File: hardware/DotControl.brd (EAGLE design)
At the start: 30.7 x 65 mm, 24 parts, among them CN1 1X4-BIG, J3 USB-MICROB, SW2 Previous, SW5 Previous, SW6 Next, SW8 Ok, U1 ATMEGA328P-MU-QFN32, U2 TMP102

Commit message: Minor rearrange wires
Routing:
- net +3V3: track 156.8 -> 151.4 mm
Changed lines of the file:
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@@
 <layer number="14" name="Route14" color="1" fill="6" visible="no" active="no"/>
 <layer number="15" name="Route15" color="4" fill="6" visible="no" active="no"/>
-<layer number="16" name="Bottom" color="1" fill="1" visible="no" active="yes"/>
+<layer number="16" name="Bottom" color="1" fill="1" visible="yes" active="yes"/>
 <layer number="17" name="Pads" color="2" fill="1" visible="yes" active="yes"/>
 <layer number="18" name="Vias" color="2" fill="1" visible="yes" active="yes"/>
@@
 <layer number="20" name="Dimension" color="15" fill="1" visible="yes" active="yes"/>
 <layer number="21" name="tPlace" color="7" fill="1" visible="yes" active="yes"/>
-<layer number="22" name="bPlace" color="7" fill="1" visible="no" active="yes"/>
-<layer number="23" name="tOrigins" color="15" fill="1" visible="no" active="yes"/>
-<layer number="24" name="bOrigins" color="15" fill="1" visible="no" active="yes"/>
+<layer number="22" name="bPlace" color="7" fill="1" visible="yes" active="yes"/>
+<layer number="23" name="tOrigins" color="15" fill="1" visible="yes" active="yes"/>
+<layer number="24" name="bOrigins" color="15" fill="1" visible="yes" active="yes"/>
 <layer number="25" name="tNames" color="7" fill="1" visible="no" active="yes"/>
 <layer number="26" name="bNames" color="7" fill="1" visible="no" active="yes"/>
@@
 <wire x1="16.891" y1="12.7762" x2="16.5862" y2="13.081" width="0.1524" layer="1"/>
 <wire x1="16.5862" y1="13.081" x2="16.4338" y2="13.081" width="0.1524" layer="1"/>
-<wire x1="19.6592" y1="13.6318" x2="19.194" y2="14.097" width="0.1524" layer="16"/>
-<wire x1="19.194" y1="14.097" x2="18.7452" y2="14.097" width="0.1524" layer="16"/>
+<wire x1="19.6592" y1="13.6318" x2="19.2194" y2="14.0716" width="0.1524" layer="16"/>
 <wire x1="16.8652" y1="13.5124" x2="17.3732" y2="13.5124" width="0.1524" layer="16"/>
 <wire x1="17.3732" y1="13.5124" x2="17.9324" y2="14.0716" width="0.1524" layer="16"/>
-<wire x1="17.9324" y1="14.0716" x2="18.7198" y2="14.0716" width="0.1524" layer="16"/>
-<wire x1="18.7198" y1="14.0716" x2="18.7452" y2="14.097" width="0.1524" layer="16"/>
+<wire x1="17.9324" y1="14.0716" x2="19.2194" y2="14.0716" width="0.1524" layer="16"/>
 </signal>
 <signal name="RST">
@@
 <contactref element="R7" pad="5"/>
 <contactref element="SJ1" pad="2"/>
-<wire x1="26.0604" y1="39.624" x2="26.0604" y2="41.6052" width="0.1524" layer="16"/>
-<wire x1="26.0604" y1="41.6052" x2="26.0604" y2="42.672" width="0.1524" layer="16"/>
-<wire x1="26.9748" y1="38.7096" x2="26.0604" y2="39.624" width="0.1524" layer="16"/>
-<wire x1="26.9748" y1="38.2524" x2="26.9748" y2="38.7096" width="0.1524" layer="16"/>
-<wire x1="26.8224" y1="38.1" x2="26.9748" y2="38.2524" width="0.1524" layer="16"/>
-<wire x1="26.9748" y1="37.9476" x2="26.8224" y2="38.1" width="0.1524" layer="16"/>
 <wire x1="3.2004" y1="61.4172" x2="3.2004" y2="61.8744" width="0.1524" layer="1"/>
 <wire x1="3.6576" y1="60.96" x2="3.2004" y2="61.4172" width="0.1524" layer="1"/>
@@
 <wire x1="12.4968" y1="55.0164" x2="10.0584" y2="55.0164" width="0.1524" layer="1"/>
 <wire x1="25.908" y1="41.6052" x2="12.4968" y2="55.0164" width="0.1524" layer="1"/>
-<wire x1="26.0604" y1="41.6052" x2="25.908" y2="41.6052" width="0.1524" layer="16"/>
 <wire x1="3.2004" y1="61.8744" x2="3.1225" y2="61.9" width="0.1524" layer="1"/>
 <wire x1="13.8684" y1="23.7744" x2="13.2588" y2="23.7744" width="0.1524" layer="16"/>

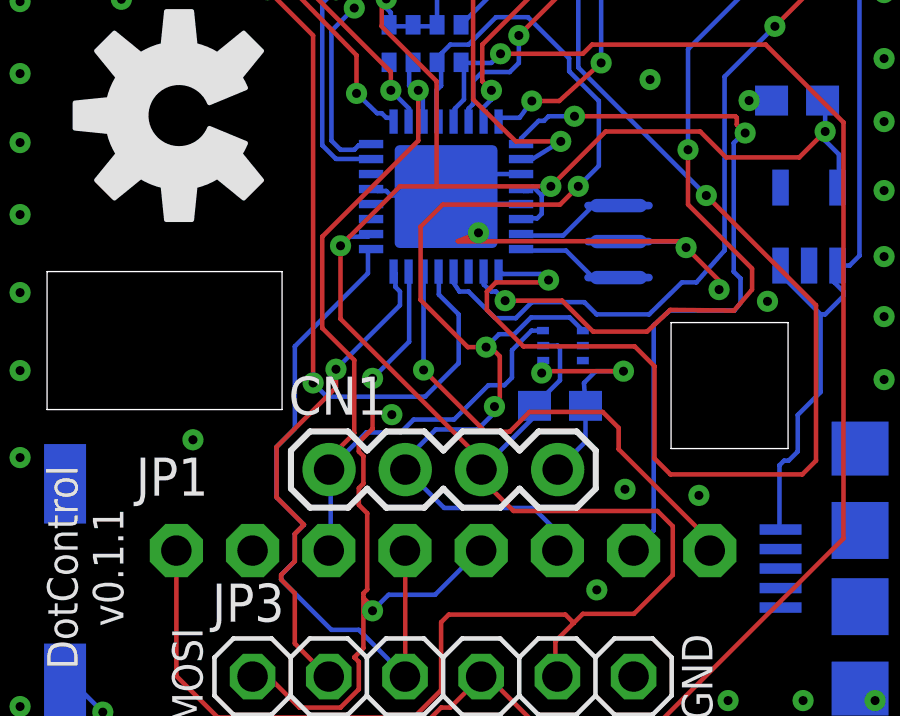
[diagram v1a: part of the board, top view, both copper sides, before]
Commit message: Improve routing and vias
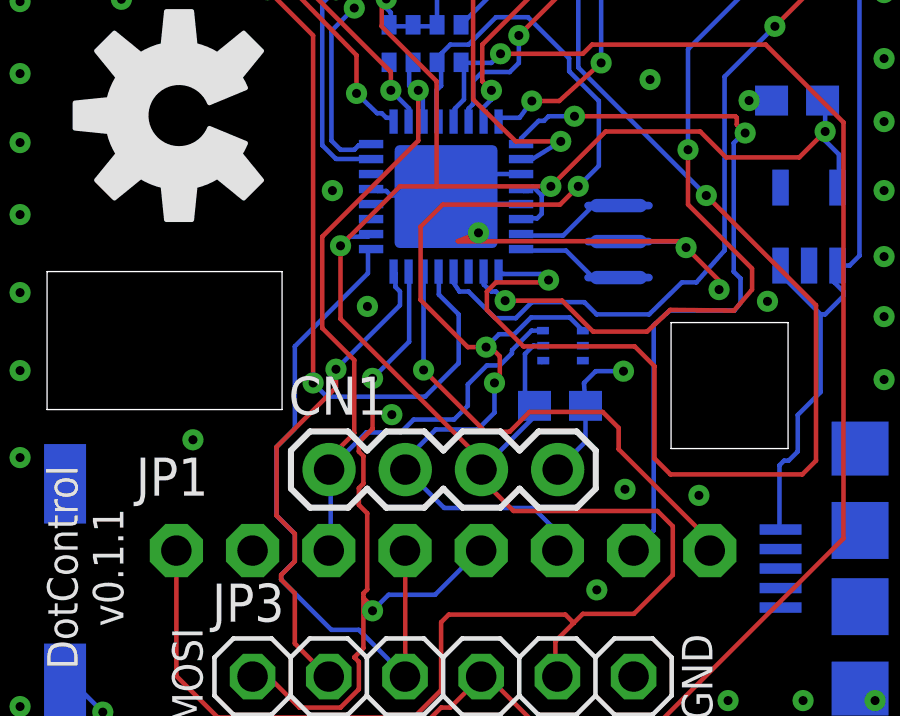
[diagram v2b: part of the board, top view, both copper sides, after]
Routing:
- net GND: track 34.6 -> 31.5 mm, vias 103 -> 104
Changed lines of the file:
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@@
 <wire x1="15.4432" y1="17.0372" x2="16.256" y2="17.85" width="0.1524" layer="16"/>
 <wire x1="18.3392" y1="12.6318" x2="18.288" y2="12.5806" width="0.1524" layer="16"/>
-<wire x1="18.288" y1="12.5806" x2="18.288" y2="12.2174" width="0.1524" layer="16"/>
-<via x="18.288" y="12.2174" extent="1-16" drill="0.3"/>
-<wire x1="18.288" y1="12.2174" x2="18.35" y2="12.2794" width="0.1524" layer="1"/>
-<wire x1="18.35" y1="12.2794" x2="21.0132" y2="12.2794" width="0.1524" layer="1"/>
 <wire x1="19.6968" y1="11.8876" x2="20.0886" y2="12.2794" width="0.1524" layer="16"/>
 <wire x1="20.0886" y1="12.2794" x2="21.0132" y2="12.2794" width="0.1524" layer="16"/>
+<via x="12.4788" y="14.4384" extent="1-16" drill="0.3"/>
+<via x="11.3104" y="18.2992" extent="1-16" drill="0.3"/>
 <wire x1="16.256" y1="17.85" x2="16.1798" y2="17.8308" width="0" layer="19" extent="16-16"/>
 </signal>
@@
 <wire x1="10.0584" y1="10.3632" x2="10.0584" y2="13.1064" width="0.1524" layer="16"/>
 <wire x1="9.4488" y1="9.7536" x2="10.0584" y2="10.3632" width="0.1524" layer="16"/>
-<wire x1="9.4488" y1="8.0772" x2="9.4488" y2="9.7536" width="0.1524" layer="16"/>
-<wire x1="10.3632" y1="7.1628" x2="9.4488" y2="8.0772" width="0.1524" layer="16"/>
-<wire x1="10.0584" y1="6.858" x2="10.3632" y2="7.1628" width="0.1524" layer="16"/>
+<wire x1="9.4488" y1="7.4676" x2="9.4488" y2="9.7536" width="0.1524" layer="16"/>
 <wire x1="10.0584" y1="5.9436" x2="10.0584" y2="6.858" width="0.1524" layer="16"/>
 <wire x1="9.6012" y1="5.4864" x2="10.0584" y2="5.9436" width="0.1524" layer="16"/>
@@
 <wire x1="12.4968" y1="16.3068" x2="12.6" y2="16.35" width="0.1524" layer="16"/>
 <wire x1="13.716" y1="2.1336" x2="13.73" y2="2.1" width="0.1524" layer="16"/>
+<wire x1="9.4488" y1="7.4676" x2="10.0584" y2="6.858" width="0.1524" layer="16"/>
 </signal>
 <signal name="MISO">
@@
 <wire x1="13.5636" y1="14.9352" x2="13.4112" y2="15.0876" width="0.1524" layer="16"/>
 <wire x1="13.5636" y1="14.478" x2="13.5636" y2="14.9352" width="0.1524" layer="16"/>
-<wire x1="11.43" y1="12.3444" x2="13.5636" y2="14.478" width="0.1524" layer="16"/>
 <wire x1="11.43" y1="11.7348" x2="11.43" y2="12.3444" width="0.1524" layer="1"/>
 <wire x1="9.4488" y1="9.7536" x2="11.43" y2="11.7348" width="0.1524" layer="1"/>
-<wire x1="9.4488" y1="8.0772" x2="9.4488" y2="9.7536" width="0.1524" layer="1"/>
-<wire x1="10.3632" y1="7.1628" x2="9.4488" y2="8.0772" width="0.1524" layer="1"/>
-<wire x1="10.0584" y1="6.858" x2="10.3632" y2="7.1628" width="0.1524" layer="1"/>
+<wire x1="9.4488" y1="7.4676" x2="9.4488" y2="9.7536" width="0.1524" layer="1"/>
 <wire x1="10.0584" y1="5.9436" x2="10.0584" y2="6.858" width="0.1524" layer="1"/>
 <wire x1="9.6012" y1="5.4864" x2="10.0584" y2="5.9436" width="0.1524" layer="1"/>
@@
 <wire x1="11.1252" y1="2.1336" x2="11.19" y2="2.1" width="0.1524" layer="1"/>
 <via x="11.43" y="12.3444" extent="1-16" drill="0.3"/>
+<wire x1="11.43" y1="12.3444" x2="13.5636" y2="14.478" width="0.1524" layer="16"/>
+<wire x1="9.4488" y1="7.4676" x2="10.0584" y2="6.858" width="0.1524" layer="1"/>
 </signal>
 <signal name="SDA">
@@
 <contactref element="U2" pad="6"/>
 <wire x1="12.4362" y1="10.2362" x2="11.2" y2="9" width="0.1524" layer="16"/>
-<wire x1="17.2974" y1="12.065" x2="17.0434" y2="11.811" width="0.1524" layer="16"/>
-<wire x1="17.0434" y1="11.811" x2="16.51" y2="11.811" width="0.1524" layer="16"/>
-<wire x1="16.51" y1="11.811" x2="15.367" y2="10.668" width="0.1524" layer="16"/>
 <wire x1="15.367" y1="10.668" x2="14.0208" y2="10.668" width="0.1524" layer="16"/>
 <wire x1="14.0208" y1="10.668" x2="13.589" y2="10.2362" width="0.1524" layer="16"/>
@@
 <wire x1="17.9498" y1="13.6318" x2="18.3292" y2="13.6318" width="0.1524" layer="16"/>
 <wire x1="17.9498" y1="13.6318" x2="17.2974" y2="12.9794" width="0.1524" layer="16"/>
-<wire x1="17.2974" y1="12.9794" x2="17.2974" y2="12.065" width="0.1524" layer="16"/>
+<wire x1="17.2974" y1="12.9794" x2="17.2974" y2="12.8778" width="0.1524" layer="16"/>
+<wire x1="17.2974" y1="12.8778" x2="16.891" y2="12.4714" width="0.1524" layer="16"/>
+<wire x1="16.891" y1="12.4714" x2="16.4592" y2="12.4714" width="0.1524" layer="16"/>
+<wire x1="16.4592" y1="12.4714" x2="15.8242" y2="11.8364" width="0.1524" layer="16"/>
+<wire x1="15.8242" y1="11.8364" x2="15.8242" y2="11.1252" width="0.1524" layer="16"/>
+<wire x1="15.8242" y1="11.1252" x2="15.367" y2="10.668" width="0.1524" layer="16"/>
 </signal>
 <signal name="SCL">
@@
 <wire x1="14.7574" y1="10.3378" x2="16.1544" y2="10.3378" width="0.1524" layer="16"/>
 <wire x1="16.1544" y1="10.3378" x2="16.7132" y2="10.8966" width="0.1524" layer="16"/>
-<wire x1="16.7132" y1="10.8966" x2="16.7132" y2="11.0998" width="0.1524" layer="16"/>
-<via x="16.7132" y="11.0998" extent="1-16" drill="0.3"/>
-<wire x1="16.7132" y1="11.0998" x2="16.891" y2="11.2776" width="0.1524" layer="1"/>
-<wire x1="16.891" y1="11.2776" x2="16.891" y2="12.7762" width="0.1524" layer="1"/>
-<wire x1="16.891" y1="12.7762" x2="16.5862" y2="13.081" width="0.1524" layer="1"/>
+<wire x1="16.7132" y1="10.8966" x2="16.7132" y2="11.8872" width="0.1524" layer="16"/>
+<via x="16.7132" y="11.8872" extent="1-16" drill="0.3"/>
 <wire x1="16.5862" y1="13.081" x2="16.4338" y2="13.081" width="0.1524" layer="1"/>
 <wire x1="19.6592" y1="13.6318" x2="19.2194" y2="14.0716" width="0.1524" layer="16"/>
@@
 <wire x1="17.3732" y1="13.5124" x2="17.9324" y2="14.0716" width="0.1524" layer="16"/>
 <wire x1="17.9324" y1="14.0716" x2="19.2194" y2="14.0716" width="0.1524" layer="16"/>
+<wire x1="16.891" y1="12.7762" x2="16.5862" y2="13.081" width="0.1524" layer="1"/>
+<wire x1="16.891" y1="12.7762" x2="16.891" y2="12.065" width="0.1524" layer="1"/>
+<wire x1="16.891" y1="12.065" x2="16.7132" y2="11.8872" width="0.1524" layer="1"/>
 </signal>
 <signal name="RST">
@@
 <contactref element="C3" pad="1"/>
 <contactref element="U2" pad="5"/>
-<wire x1="18.8976" y1="11.9752" x2="18.0476" y2="11.1252" width="0.1524" layer="16"/>
 <wire x1="18.0476" y1="11.1252" x2="18.0476" y2="10.7676" width="0.1524" layer="16"/>
 <wire x1="18.0476" y1="10.7676" x2="16.28" y2="9" width="0.1524" layer="16"/>
@@
 <wire x1="15.1892" y1="4.1656" x2="19.0754" y2="4.1656" width="0.1524" layer="1"/>
 <wire x1="19.0754" y1="4.1656" x2="19.3548" y2="3.8862" width="0.1524" layer="1"/>
-<wire x1="18.8976" y1="11.9752" x2="18.8976" y2="13.0556" width="0.1524" layer="16"/>
-<wire x1="18.8976" y1="13.0556" x2="18.8214" y2="13.1318" width="0.1524" layer="16"/>
-<wire x1="18.8214" y1="13.1318" x2="18.3392" y2="13.1318" width="0.1524" layer="16"/>
+<wire x1="18.3392" y1="13.1318" x2="18.0086" y2="13.1318" width="0.1524" layer="16"/>
+<wire x1="18.0086" y1="13.1318" x2="17.7292" y2="12.8524" width="0.1524" layer="16"/>
+<wire x1="17.7292" y1="12.8524" x2="17.7292" y2="11.4436" width="0.1524" layer="16"/>
+<wire x1="17.7292" y1="11.4436" x2="18.0476" y2="11.1252" width="0.1524" layer="16"/>
 </signal>
 <signal name="PUSH">
@@
 <wire x1="17.8816" y1="10.922" x2="17.2212" y2="10.2616" width="0.1524" layer="1"/>
 <wire x1="17.2212" y1="10.2616" x2="16.4084" y2="10.2616" width="0.1524" layer="1"/>
-<wire x1="16.4084" y1="10.2616" x2="14.351" y2="12.319" width="0.1524" layer="1"/>
 <via x="14.351" y="12.319" extent="1-16" drill="0.3"/>
 <wire x1="14.351" y1="12.319" x2="14.351" y2="15.599" width="0.1524" layer="16"/>
 <wire x1="14.351" y1="15.599" x2="14.35" y2="15.6" width="0.1524" layer="16"/>
+<wire x1="16.4084" y1="10.2616" x2="14.351" y2="12.319" width="0.1524" layer="1"/>
 </signal>
 <signal name="N$6">

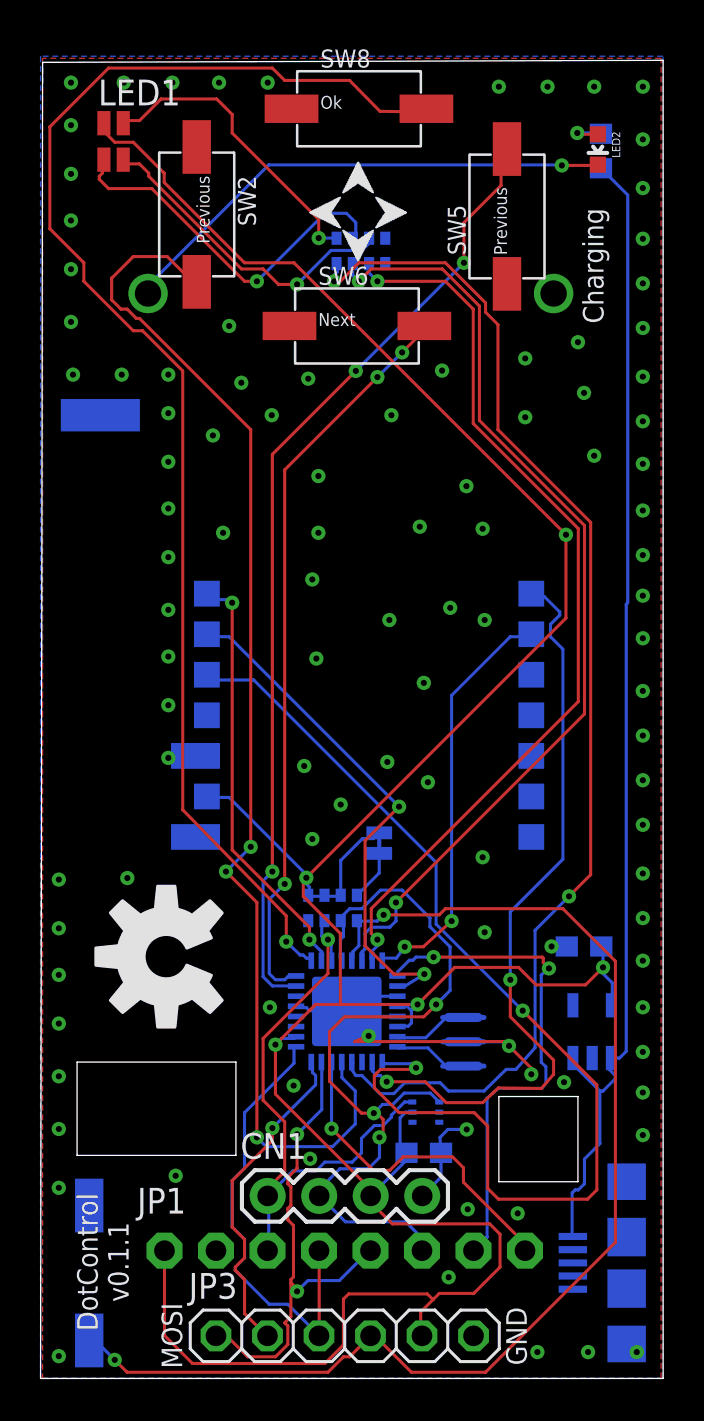
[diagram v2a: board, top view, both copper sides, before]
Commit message: Add rounded corners
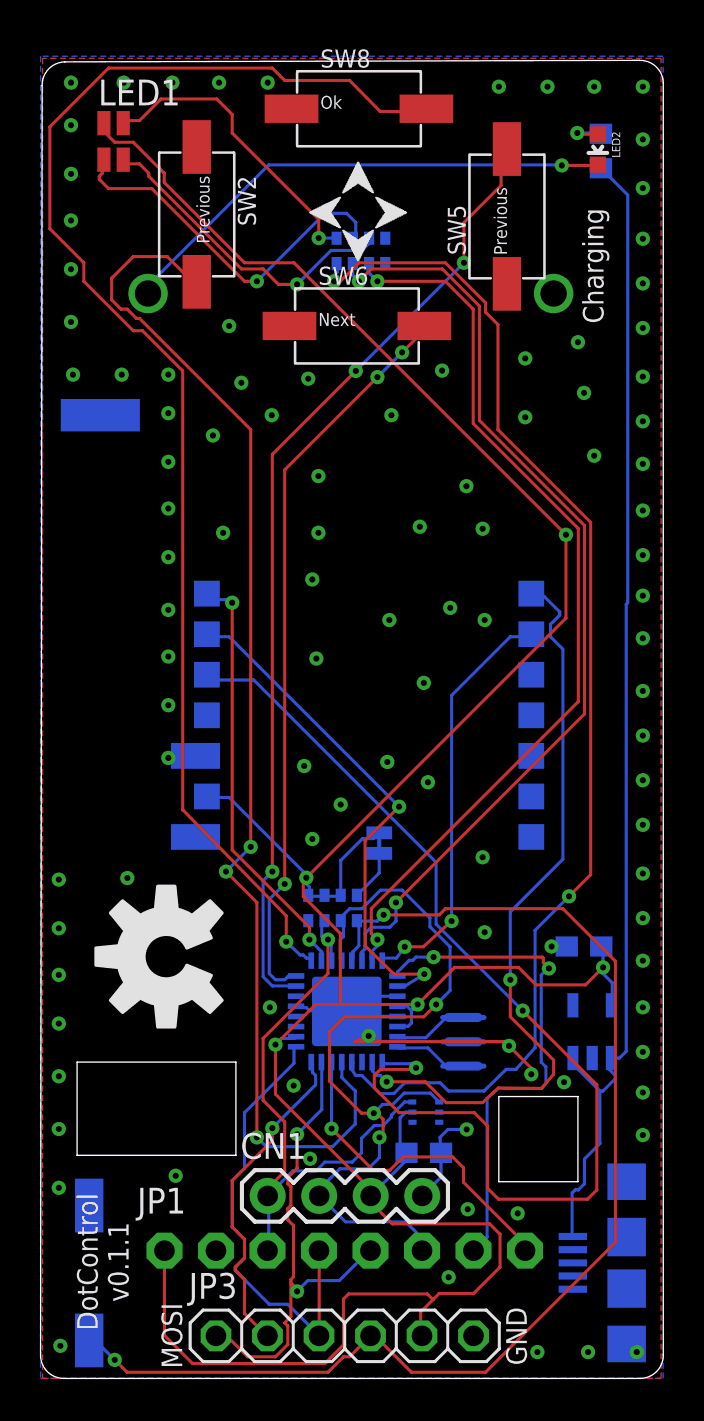
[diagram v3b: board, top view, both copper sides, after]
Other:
- outline, holes or cut-outs redrawn
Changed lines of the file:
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@@
 <board>
 <plain>
-<wire x1="0" y1="0" x2="30.7" y2="0" width="0" layer="20"/>
-<wire x1="30.7" y1="0" x2="30.7" y2="65" width="0" layer="20"/>
-<wire x1="30.7" y1="65" x2="0.1" y2="64.9" width="0" layer="20"/>
-<wire x1="0.1" y1="64.9" x2="0" y2="0" width="0" layer="20"/>
+<wire x1="1.1684" y1="0" x2="29.591" y2="0" width="0" layer="20"/>
 <rectangle x1="1" y1="46.7" x2="4.9" y2="48.3" layer="16"/>
 <wire x1="22.6" y1="13.9" x2="26.5" y2="13.9" width="0.01" layer="20"/>
@@
 <text x="-10.4648" y="71.0438" size="1.778" layer="48">Display should be 3.3V compatible. Check if solderjumper J1
 on it should be soldered to bypass voltage regulator.</text>
+<wire x1="1.1684" y1="0" x2="0" y2="1.1176" width="0.001" layer="20" curve="-90"/>
+<wire x1="30.7086" y1="1.1684" x2="29.591" y2="0" width="0.001" layer="20" curve="-90"/>
+<wire x1="29.5402" y1="64.9986" x2="30.7086" y2="63.881" width="0.001" layer="20" curve="-90"/>
+<wire x1="0.0762" y1="63.754" x2="1.1938" y2="64.9224" width="0.001" layer="20" curve="-90"/>
+<wire x1="1.1938" y1="64.9224" x2="29.5402" y2="64.9986" width="0.001" layer="20"/>
+<wire x1="30.7086" y1="63.881" x2="30.7086" y2="1.1684" width="0.001" layer="20"/>
+<wire x1="0" y1="1.1176" x2="0.0762" y2="63.754" width="0.001" layer="20"/>
 </plain>
 <attributes>
@@
 <via x="24.5" y="1.3" extent="1-16" drill="0.3"/>
 <via x="27" y="1.3" extent="1-16" drill="0.3"/>
-<via x="0.9" y="1.1" extent="1-16" drill="0.3"/>
+<via x="0.9762" y="1.608" extent="1-16" drill="0.3"/>
 <polygon width="0.4064" layer="1">
 <vertex x="0.1" y="0"/>
